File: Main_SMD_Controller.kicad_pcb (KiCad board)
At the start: 2 copper layers, 65 x 85 mm, 49 parts, among them J1 2.1-5.5 +12VDC, J10 Vin_-, J11 Conn_01x02, J12 Vsens, J13 Vin+, J2 Switch_Control, J3 +5V, J4 AnalogIO, J5 +12V, J6 VsensJMP, J7 Drain, J8 Gate, J9 Source, P1 Eoshi-chan_Silk, P2 Eoshi-chan_Silk, P3 Serial_QR, Q1 2N7002K, U1 NJM7805SDL1, U2 TC74HC4066AF(F), U3 AD8226ARZ, U4 S-89713B-K8T2U

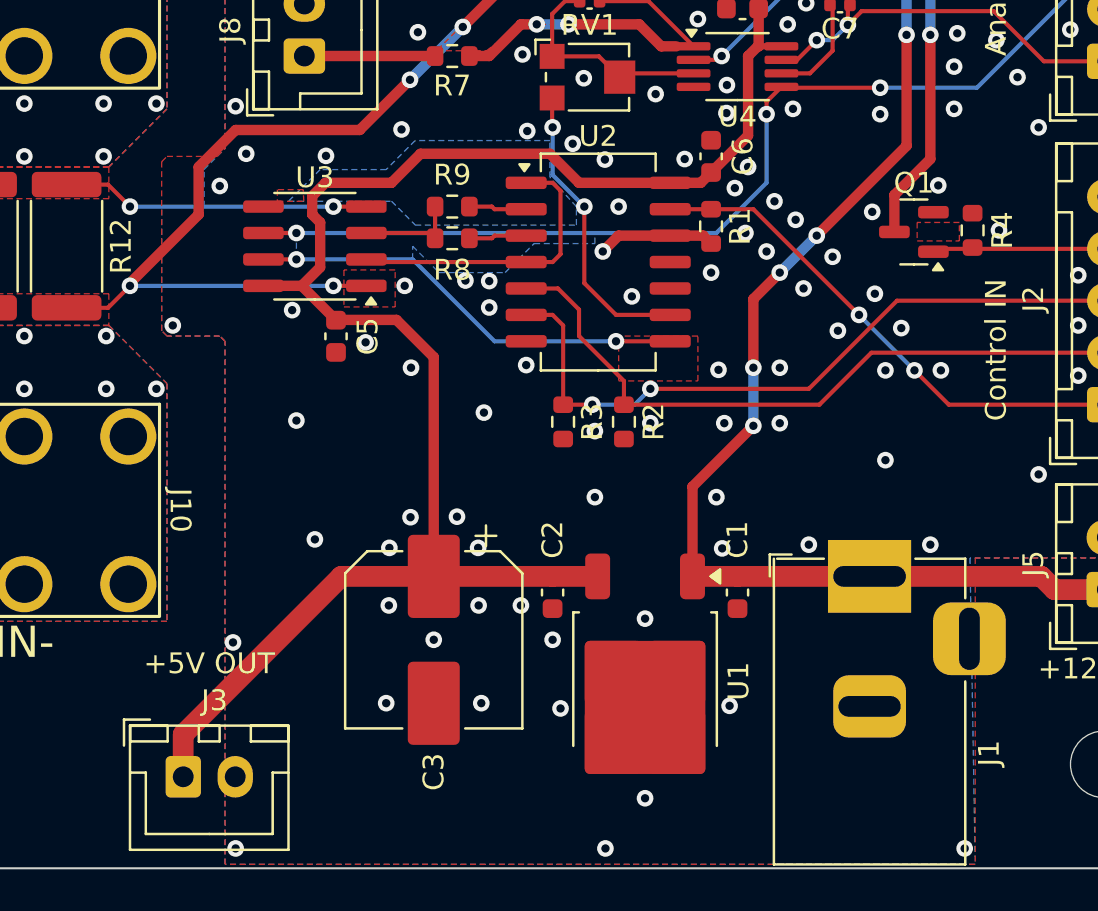
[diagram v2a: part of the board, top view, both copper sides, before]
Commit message: Add negative power
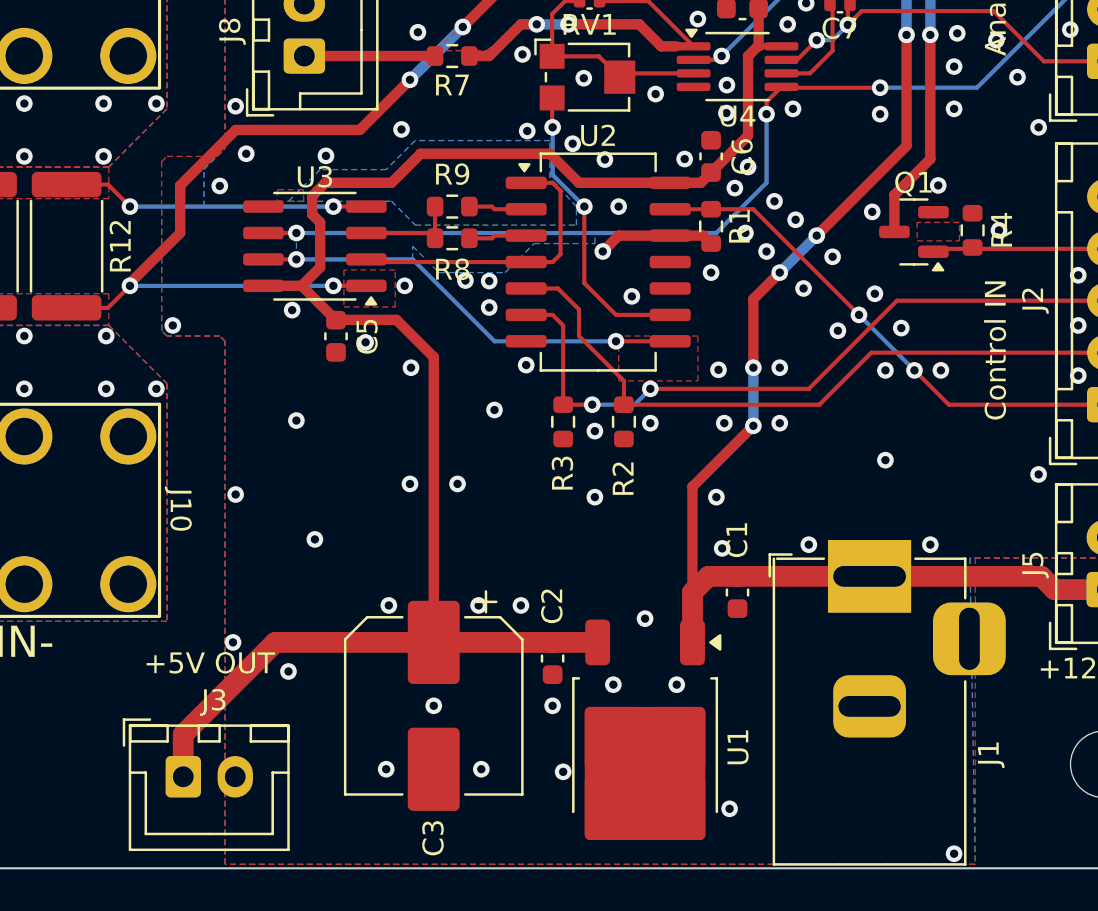
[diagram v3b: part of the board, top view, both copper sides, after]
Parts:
- moved C2 3.18 mm to (63.5, 104.9)
- moved U1 3.18 mm to (67.9, 109.2)
- moved C3 3.17 mm to (57.8, 107.2)
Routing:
- net +12V: track 112.6 -> 116.1 mm
- net VCC: track 80.9 -> 82.7 mm
- net GND: vias 117 -> 116
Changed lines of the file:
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@@
 	(footprint "Package_TO_SOT_SMD:TO-252-2"
 		(layer "F.Cu")
-		(at 67.945 106.005 -90)
+		(at 67.945 109.18 -90)
 		(descr "TO-252/DPAK SMD package, http://www.infineon.com/cms/en/product/packages/PG-TO252/PG-TO252-3-1/")
 		(tags "DPAK TO-252 DPAK-3 TO-252-3 SOT-428")
@@
 		(tags "resistor")
 		(property "Reference" "R2"
-			(at 0 -1.43 90)
+			(at 2.731 0 90)
 			(layer "F.SilkS")
 			(effects
@@
 	(footprint "Capacitor_SMD:CP_Elec_8x6.2"
 		(layer "F.Cu")
-		(at 57.785 104.015 -90)
+		(at 57.785 107.19 -90)
 		(descr "SMD capacitor, aluminum electrolytic, Nichicon, 8.0x6.2mm")
 		(tags "capacitor electrolytic")
@@
 		(tags "resistor")
 		(property "Reference" "R3"
-			(at 0 -1.397 90)
+			(at 2.477 0 90)
 			(layer "F.SilkS")
 			(effects
@@
 	(footprint "Capacitor_SMD:C_0603_1608Metric"
 		(layer "F.Cu")
-		(at 63.5 101.74 -90)
+		(at 63.5 104.915 -90)
 		(descr "Capacitor SMD 0603 (1608 Metric), square (rectangular) end terminal, IPC_7351 nominal, (Body size source: IPC-SM-782 page 76, https://www.pcb-3d.com/wordpress/wp-content/uploads/ipc-sm-782a_amendment_1_and_2.pdf), generated with kicad-footprint-generator")
 		(tags "capacitor")
@@
 	)
 	(segment
-		(start 51.435 86.995)
-		(end 53.073 88.633)
+		(start 57.785 90.424)
+		(end 57.785 104.14)
 		(width 0.5)
 		(layer "F.Cu")
@@
 	)
 	(segment
-		(start 53.34 100.965)
-		(end 57.785 100.965)
-		(width 1)
-		(layer "F.Cu")
-		(net 1)
-	)
-	(segment
 		(start 51.943 82.677)
 		(end 52.578 82.042)
@@
 	)
 	(segment
-		(start 45.74 108.565)
-		(end 53.34 100.965)
+		(start 45.74 110.6)
+		(end 45.74 108.565)
 		(width 1)
 		(layer "F.Cu")
@@
 	)
 	(segment
-		(start 57.785 100.965)
-		(end 63.5 100.965)
-		(width 1)
+		(start 49.595 86.995)
+		(end 51.435 86.995)
+		(width 0.5)
 		(layer "F.Cu")
 		(net 1)
 	)
 	(segment
-		(start 63.5 100.965)
-		(end 65.665 100.965)
-		(width 1)
+		(start 51.435 86.995)
+		(end 52.324 86.106)
+		(width 0.5)
 		(layer "F.Cu")
 		(net 1)
 	)
 	(segment
-		(start 57.785 90.424)
-		(end 57.785 100.965)
+		(start 51.435 86.995)
+		(end 53.073 88.633)
 		(width 0.5)
 		(layer "F.Cu")
@@
 	)
 	(segment
-		(start 49.595 86.995)
-		(end 51.435 86.995)
-		(width 0.5)
+		(start 63.5 104.14)
+		(end 57.785 104.14)
+		(width 1)
 		(layer "F.Cu")
 		(net 1)
 	)
 	(segment
-		(start 51.435 86.995)
-		(end 52.324 86.106)
+		(start 55.753 82.042)
+		(end 57.15 80.645)
 		(width 0.5)
 		(layer "F.Cu")
@@
 	)
 	(segment
-		(start 55.753 82.042)
-		(end 57.15 80.645)
-		(width 0.5)
+		(start 45.74 108.565)
+		(end 50.165 104.14)
+		(width 1)
 		(layer "F.Cu")
 		(net 1)
@@
 	)
 	(segment
+		(start 65.665 104.14)
+		(end 63.5 104.14)
+		(width 1)
+		(layer "F.Cu")
+		(net 1)
+	)
+	(segment
 		(start 73.365 75.479)
 		(end 72.898 75.946)
@@
 	)
 	(segment
-		(start 45.74 110.6)
-		(end 45.74 108.565)
-		(width 1)
+		(start 73.406 75.479)
+		(end 74.5025 75.479)
+		(width 0.3)
 		(layer "F.Cu")
 		(net 1)
 	)
 	(segment
-		(start 73.406 75.479)
-		(end 74.5025 75.479)
-		(width 0.3)
+		(start 50.165 104.14)
+		(end 57.785 104.14)
+		(width 1)
 		(layer "F.Cu")
 		(net 1)
@@
 	)
 	(via
-		(at 55.6514 99.5934)
+		(at 56.642 96.52)
 		(size 0.8)
 		(drill 0.4)
@@
 	)
 	(via
-		(at 60.198 93.091)
+		(at 60.706 92.964)
 		(size 0.8)
 		(drill 0.4)
@@
 	)
 	(via
-		(at 60.071 107.061)
+		(at 60.071 110.236)
 		(size 0.8)
 		(drill 0.4)
@@
 	)
 	(via
-		(at 48.26 114.046)
+		(at 50.8 105.537)
 		(size 0.8)
 		(drill 0.4)
@@
 	)
 	(via
-		(at 63.881 107.315)
+		(at 63.5 107.188)
 		(size 0.8)
 		(drill 0.4)
@@
 	)
 	(via
-		(at 58.9026 98.0948)
+		(at 58.928 96.52)
 		(size 0.8)
 		(drill 0.4)
@@
 	)
 	(via
-		(at 57.785 104.013)
+		(at 55.499 110.236)
 		(size 0.8)
 		(drill 0.4)
@@
 	)
 	(via
-		(at 55.499 107.061)
+		(at 57.785 107.188)
 		(size 0.8)
 		(drill 0.4)
@@
 	)
 	(via
-		(at 67.945 111.633)
+		(at 69.469 106.172)
 		(size 0.8)
 		(drill 0.4)
@@
 	)
 	(via
-		(at 63.5 104.013)
+		(at 64.008 110.363)
 		(size 0.8)
 		(drill 0.4)
@@
 	)
 	(via
-		(at 72.009 107.188)
+		(at 72.009 112.141)
 		(size 0.8)
 		(drill 0.4)
@@
 	)
 	(via
-		(at 56.6674 98.1202)
+		(at 48.26 97.028)
 		(size 0.8)
 		(drill 0.4)
@@
 	)
 	(via
-		(at 83.312 114.046)
+		(at 82.804 114.3)
 		(size 0.8)
 		(drill 0.4)
@@
 	)
 	(via
-		(at 59.9186 99.5934)
-		(size 0.8)
-		(drill 0.4)
-		(layers "F.Cu" "B.Cu")
-		(free yes)
-		(net 2)
-	)
-	(via
 		(at 77.216 67.818)
 		(size 0.8)
@@
 	)
 	(via
-		(at 66.04 114.046)
+		(at 66.421 106.172)
 		(size 0.8)
 		(drill 0.4)
@@
 	)
 	(segment
+		(start 70.225 101.733)
+		(end 70.225 104.14)
+		(width 1)
+		(layer "F.Cu")
+		(net 19)
+	)
+	(segment
 		(start 73.152 58.42)
 		(end 59.69 58.42)
@@
 	)
 	(segment
+		(start 70.225 96.653)
+		(end 73.152 93.726)
+		(width 0.5)
+		(layer "F.Cu")
+		(net 19)
+	)
+	(segment
 		(start 54.833 63.15)
 		(end 52.57 63.15)
@@
 	)
 	(segment
-		(start 70.225 100.965)
-		(end 72.39 100.965)
-		(width 1)
+		(start 80.518 74.93)
+		(end 80.518 80.264)
+		(width 0.5)
 		(layer "F.Cu")
 		(net 19)
 	)
 	(segment
-		(start 80.518 74.93)
-		(end 80.518 80.264)
-		(width 0.5)
+		(start 70.993 100.965)
+		(end 70.225 101.733)
+		(width 1)
 		(layer "F.Cu")
 		(net 19)
@@
 	)
 	(segment
-		(start 73.152 87.63)
-		(end 74.422 86.36)
-		(width 0.5)
+		(start 72.39 100.965)
+		(end 70.993 100.965)
+		(width 1)
 		(layer "F.Cu")
 		(net 19)
 	)
 	(segment
-		(start 70.225 100.965)
-		(end 70.225 96.653)
+		(start 73.152 87.63)
+		(end 74.422 86.36)
 		(width 0.5)
 		(layer "F.Cu")
@@
 	)
 	(segment
-		(start 70.225 96.653)
-		(end 73.152 93.726)
+		(start 70.225 101.733)
+		(end 70.225 96.653)
 		(width 0.5)
 		(layer "F.Cu")
@@
 	)
 	(segment
-		(start 46.482 83.566)
-		(end 43.18 86.868)
+		(start 54.229 79.502)
+		(end 48.26 79.502)
 		(width 0.5)
 		(layer "F.Cu")
@@
 	)
 	(segment
-		(start 64.77 63.15)
-		(end 65.309 63.15)
-		(width 0.2)
+		(start 48.26 79.502)
+		(end 45.593 82.169)
+		(width 0.5)
 		(layer "F.Cu")
 		(net 27)
 	)
 	(segment
-		(start 46.482 81.28)
-		(end 46.482 83.566)
+		(start 45.593 82.169)
+		(end 45.593 84.455)
 		(width 0.5)
 		(layer "F.Cu")
@@
 	)
 	(segment
-		(start 54.229 79.502)
-		(end 48.26 79.502)
-		(width 0.5)
+		(start 64.77 63.15)
+		(end 65.309 63.15)
+		(width 0.2)
 		(layer "F.Cu")
 		(net 27)
 	)
 	(segment
-		(start 67.945 65.786)
-		(end 70.295 65.786)
+		(start 56.642 77.089)
+		(end 54.229 79.502)
 		(width 0.5)
 		(layer "F.Cu")
@@
 	)
 	(segment
-		(start 56.642 77.089)
-		(end 54.229 79.502)
+		(start 67.945 65.786)
+		(end 70.295 65.786)
 		(width 0.5)
 		(layer "F.Cu")
@@
 	)
 	(segment
-		(start 65.309 63.15)
-		(end 67.945 65.786)
+		(start 45.593 84.455)
+		(end 43.18 86.868)
 		(width 0.5)
 		(layer "F.Cu")
@@
 	)
 	(segment
-		(start 48.26 79.502)
-		(end 46.482 81.28)
+		(start 65.309 63.15)
+		(end 67.945 65.786)
 		(width 0.5)
 		(layer "F.Cu")

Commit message: alpha 2
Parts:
- removed the R8 at (58.7, 84.7)
- removed the R9 at (58.7, 83.2)
- added C1: 1u, Capacitor_SMD:C_0603_1608Metric, F.Cu at (63.2, 96.9)
- added C10: 0.1u, Capacitor_SMD:C_0603_1608Metric, F.Cu at (78.6, 82.3)
- added C3: 1u, Capacitor_SMD:C_0603_1608Metric, F.Cu at (54.0, 101.1)
- added C7: 0.1u, Capacitor_SMD:C_0603_1608Metric, F.Cu at (50.3, 80.8)
- added JP1: CLK_disable, Jumper:SolderJumper-2_P1.3mm_Open_TrianglePad1.0x1.5mm, F.Cu at (50.2, 96.0)
- added R4: 10k, Resistor_SMD:R_0603_1608Metric, F.Cu at (65.8, 94.0)
- added R5: 10k, Resistor_SMD:R_0603_1608Metric, F.Cu at (78.5, 96.8)
- added RV2: R_Potentiometer_Trim, Potentiometer_THT:Potentiometer_Bourns_3296W_Vertical, F.Cu at (63.9, 88.3)
- added RV3: R_Potentiometer_Trim, Potentiometer_THT:Potentiometer_Bourns_3296W_Vertical, F.Cu at (63.9, 82.8)
- added TP1: CLK_in, TestPoint:TestPoint_Pad_2.0x2.0mm, F.Cu at (50.2, 99.2)
- added U1: NJM4191M, Package_DMP:DMP-8_5x5_P1.27mm, F.Cu at (57.8, 97.5)
- C6: value 0.1u -> 1u
- R1: value 10k -> 20k
- R10: footprint Package_DIPSMD:DIPSMD_0W25Resistor_P10.16mm_Horizontal -> Resistor_THT:R_Axial_DIN0207_L6.3mm_D2.5mm_P10.16mm_Horizontal
- R7: renamed from R5; footprint Resistor_SMD:R_0603_1608Metric -> Resistor_THT:R_Axial_DIN0207_L6.3mm_D2.5mm_P5.08mm_Vertical
- R8: renamed from R6; footprint Resistor_SMD:R_0603_1608Metric -> Resistor_THT:R_Axial_DIN0207_L6.3mm_D2.5mm_P10.16mm_Horizontal
- RV1: footprint Potentiometer_SMD:Potentiometer_Bourns_TC33X_Vertical -> AM_Potentiometer:TSR065103R
- U3: renamed from U2; footprint Package_SO:SO-14_5.3x10.2mm_P1.27mm -> Package_DIP:DIP-14_W7.62mm
- moved C9 25.1 mm to (72.6, 73.7), turned to 180 degrees
- moved C8 25.1 mm to (53.1, 89.4), turned to -90 degrees
- moved C6 21.2 mm to (54.0, 93.2)
- moved R1 19.1 mm to (62.2, 101.1), turned to 180 degrees
- moved R3 16.5 mm to (78.6, 85.8)
- moved R8 9.38 mm to (61.8, 67.2)
- moved R7 8.42 mm to (84.9, 75.9)
- moved R2 6.65 mm to (63.9, 99.4), turned to 180 degrees
- moved U3 4.84 mm to (68.3, 81.8)
- moved RV1 4.54 mm to (60.7, 77.3)
- moved C12 3.38 mm to (68.6, 74.0)
- moved C2 3.19 mm to (72.6, 104.9)
- moved R6 2.79 mm to (86.5, 84.3)
- moved Q1 2.69 mm to (83.6, 84.4)
- moved C11 1.68 mm to (79.0, 73.4)
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- renumbered C7 to C11, C8 to C12, C1 to C2, C2 to C4, C3 to C5, C4 to C8, C5 to C9, R4 to R6, R7 to R9, U1 to U2, U3 to U4, U4 to U5
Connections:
- C6 pad 1: VCC -> VEE
- R1 pad 1: SHUNT_SELECT2 -> Net-(U1-FB)
- R1 pad 2: GND -> VEE
- R2 pad 1: SHUNT_SELECT1 -> GND
- R2 pad 2: GND -> Net-(U1-FB)
- R3 pad 1: Vconst_ENABLE -> SHUNT_SELECT2
- U4 pad 5: GND -> VEE
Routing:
- net VEE: track 0.00 -> 28.1 mm, vias 0 -> 2
- net VCC: track 82.7 -> 96.2 mm, vias 0 -> 2
- net Net-(C12-Pad1): track 10.9 -> 22.1 mm, vias 0 -> 1
- net Rg_2: track 4.93 -> 14.8 mm
- net Net-(U3-Pad8): track 21.2 -> 31.0 mm, vias 2 -> 1
- net Rg_1: track 14.4 -> 24.2 mm, vias 0 -> 1
- net Net-(RV1-Pad3): track 14.3 -> 21.8 mm, vias 2 -> 0
- net Net-(JP1-A): track 0.00 -> 7.44 mm
- net SHUNT_SELECT2: track 24.9 -> 17.7 mm
- net SHUNT_SELECT1: track 32.5 -> 25.6 mm, vias 0 -> 1
- net Net-(C11-Pad2): track 17.5 -> 22.9 mm
- net Vconst_ENABLE: track 33.8 -> 28.6 mm, vias 2 -> 3
- net +12V: track 116.1 -> 111.1 mm, vias 6 -> 0
- net Net-(U1-FB): track 0.00 -> 3.68 mm
- net Net-(C12-Pad2): track 17.3 -> 13.8 mm, vias 2 -> 0
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- added copper zone on F.Cu, net Rg_2
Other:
- board text removed: "80V, 5A, 100W"
